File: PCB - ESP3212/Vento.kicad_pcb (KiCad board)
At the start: 4 copper layers, 75.1 x 27 mm, 66 parts, among them J1 B2B-PH-K-S(LF)(SN), J2 B3B-PH-K-S(LF)(SN), J3 20021121-00010C4LF, J4 0475890001-MicroUSBPort, P1 CONN_01X18, P2 CONN_01X18, Q1 DMG2307L-7, Q2 DMG2307L-7, SW1 B3U-1000P, U1 BQ24210DQCT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

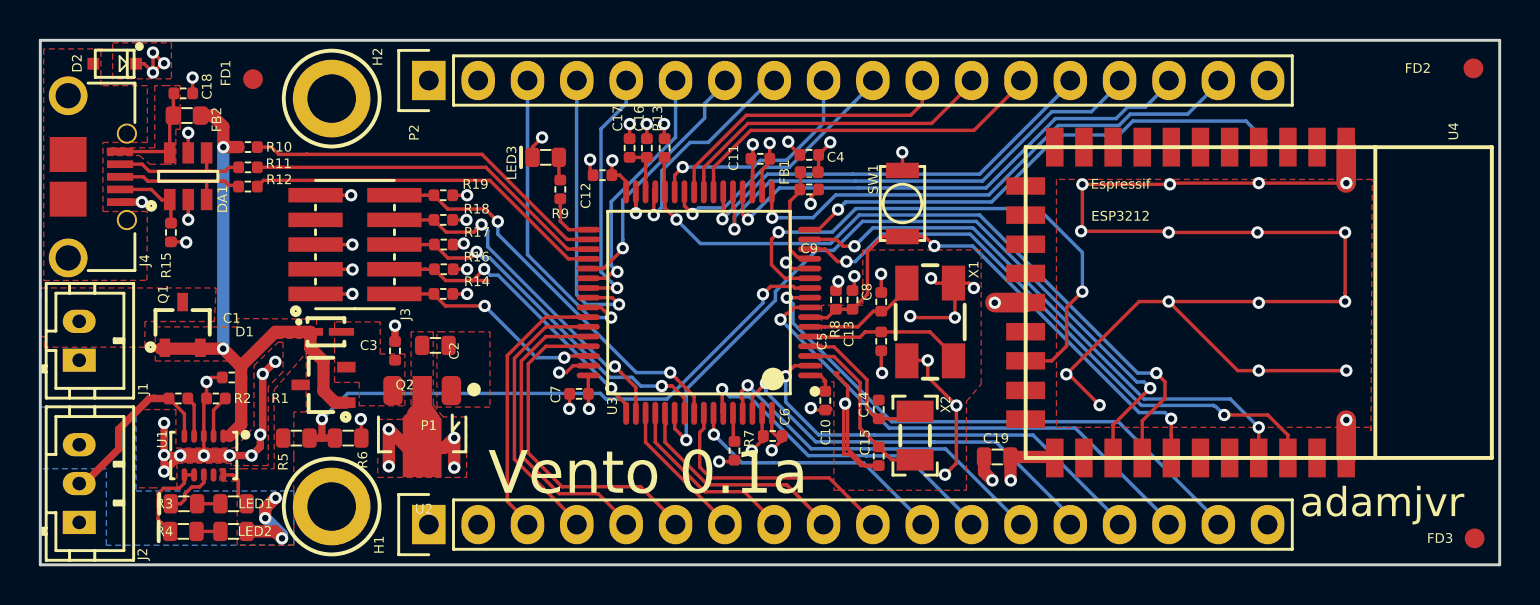
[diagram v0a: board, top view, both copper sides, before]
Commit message: Tweaks, DRC cleared, images, readme
Tweaked both designs according to the dev board scheamtics provided by
Espressif in the datasheets folder. Cleared both boards of DRC
violations, added new images and updated the readme.
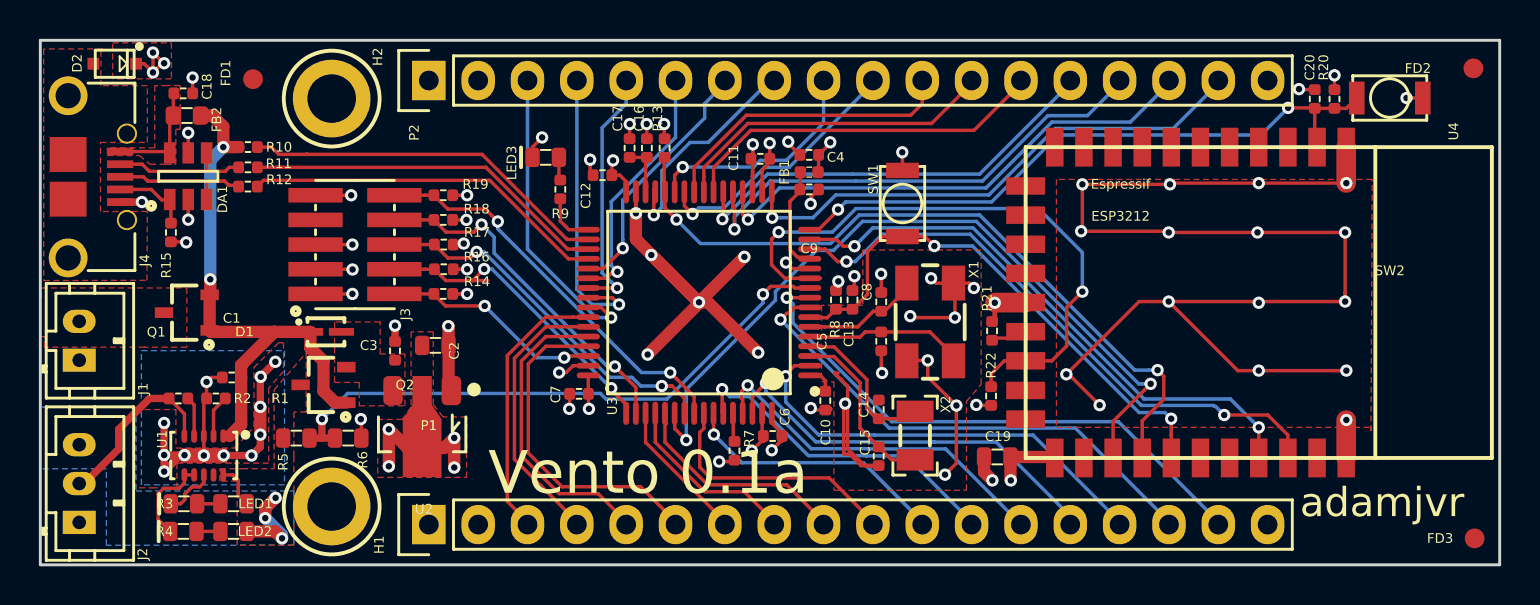
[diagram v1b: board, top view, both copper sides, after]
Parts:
- added C20: CL05B104JP5NNNC, PCB_Footprints:C0402, F.Cu at (211.5, 74.6)
- added R20: RC1005F123CS, PCB_Footprints:R0402, F.Cu at (212.5, 74.6)
- added R21: RC1005F103CS, PCB_Footprints:R0402, F.Cu at (194.9, 86.5)
- added R22: RC1005F103CS, PCB_Footprints:R0402, F.Cu at (194.8, 89.9)
- added SW2: B3U-1000P, PCB_Footprints:B3U-1000P, F.Cu at (215.3, 74.5)
- moved Q1 0.67 mm to (153.4, 85.6), turned to 180 degrees
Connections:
- C19 pad 1: Net-(C19-Pad1) -> +3V3
- U4 pad 2: Net-(U4-Pad2) -> /MCU_STM32F446RET6/STM_ESP_RST
- U4 pad 21: Net-(C19-Pad1) -> +3V3
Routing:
- net GND: track 150.3 -> 177.2 mm, vias 68 -> 77
- net /MCU_STM32F446RET6/STM_ESP_RST: track 26.3 -> 33.1 mm, vias 1 -> 2
- net +3V3: track 26.5 -> 31.5 mm, vias 17 -> 20
- net Net-(C19-Pad1): track 3.52 -> 0.00 mm, vias 1 -> 0
- net /MCU_STM32F446RET6/ESP_PGM_MODE: track 29.3 -> 32.0 mm
- net Net-(R21-Pad1): track 0.00 -> 1.91 mm
- net /MCU_STM32F446RET6/VBUS: track 31.4 -> 29.7 mm
- added copper zone on B.Cu, net GND
- removed copper zone on F.Cu, net /MCU_STM32F446RET6/VBUS
